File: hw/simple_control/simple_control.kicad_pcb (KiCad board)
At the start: 4 copper layers, 80 x 100 mm, 105 parts, among them J101 Screw_Terminal_01x02, J102 Jack-DC, J103 Screw_Terminal_01x03, J104 Screw_Terminal_01x03, J1301 Micro_SD_Card, J1401 Conn_02x05_Odd_Even, J601 Conn_01x04, J602 Raspberry_Pi_0_2_3, J603 Conn_01x03, Q1001 BC817, Q201 AOSP21357, Q701 BC817, Q801 BC817, Q901 BC817, SW1801 SW_Push, SW1901 SW_Push, SW2001 SW_Push, SW2101 SW_Push, SW602 SW_Push, U1101 CAT24C256, U1501 4050, U301 SN74AHCT125D, U601 PicoW

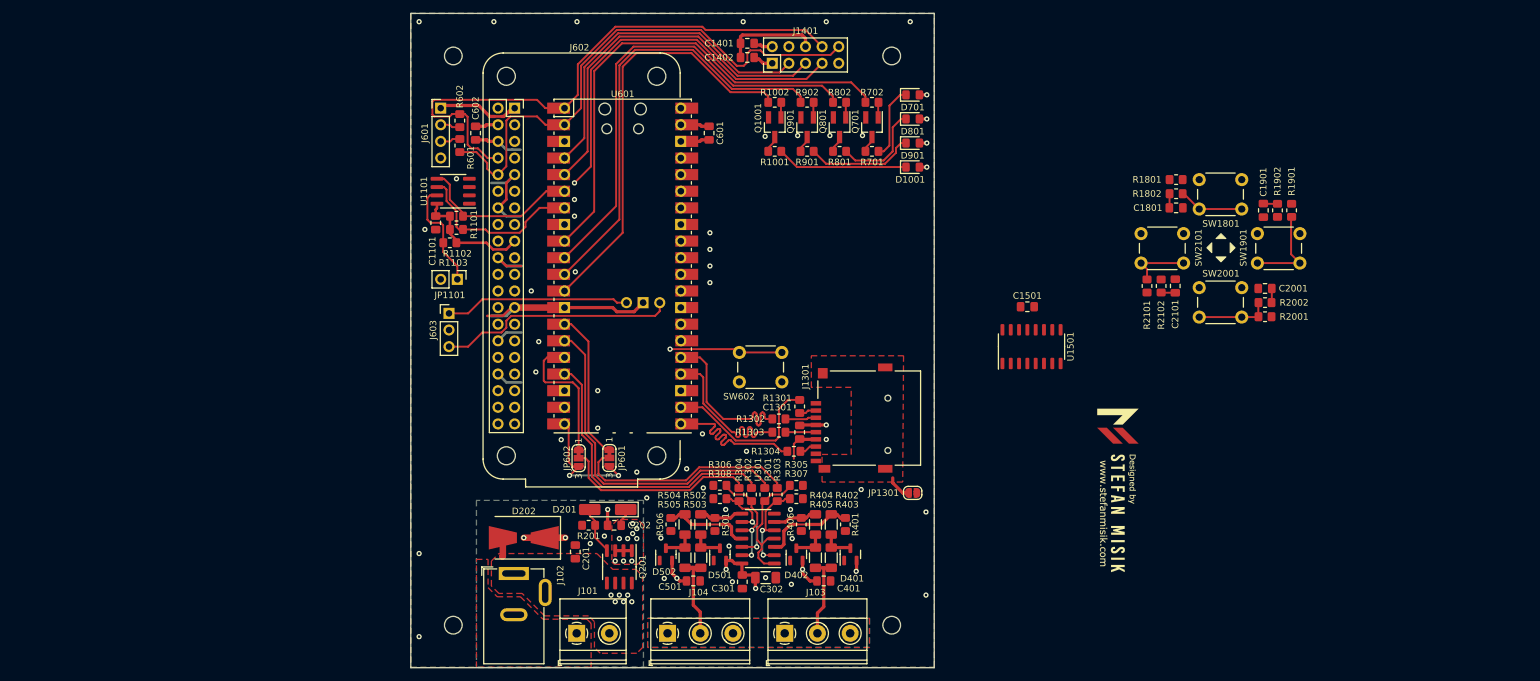
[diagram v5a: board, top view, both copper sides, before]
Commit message: chore(hw): move reset button, improve power traces, keepout near wifi antenna
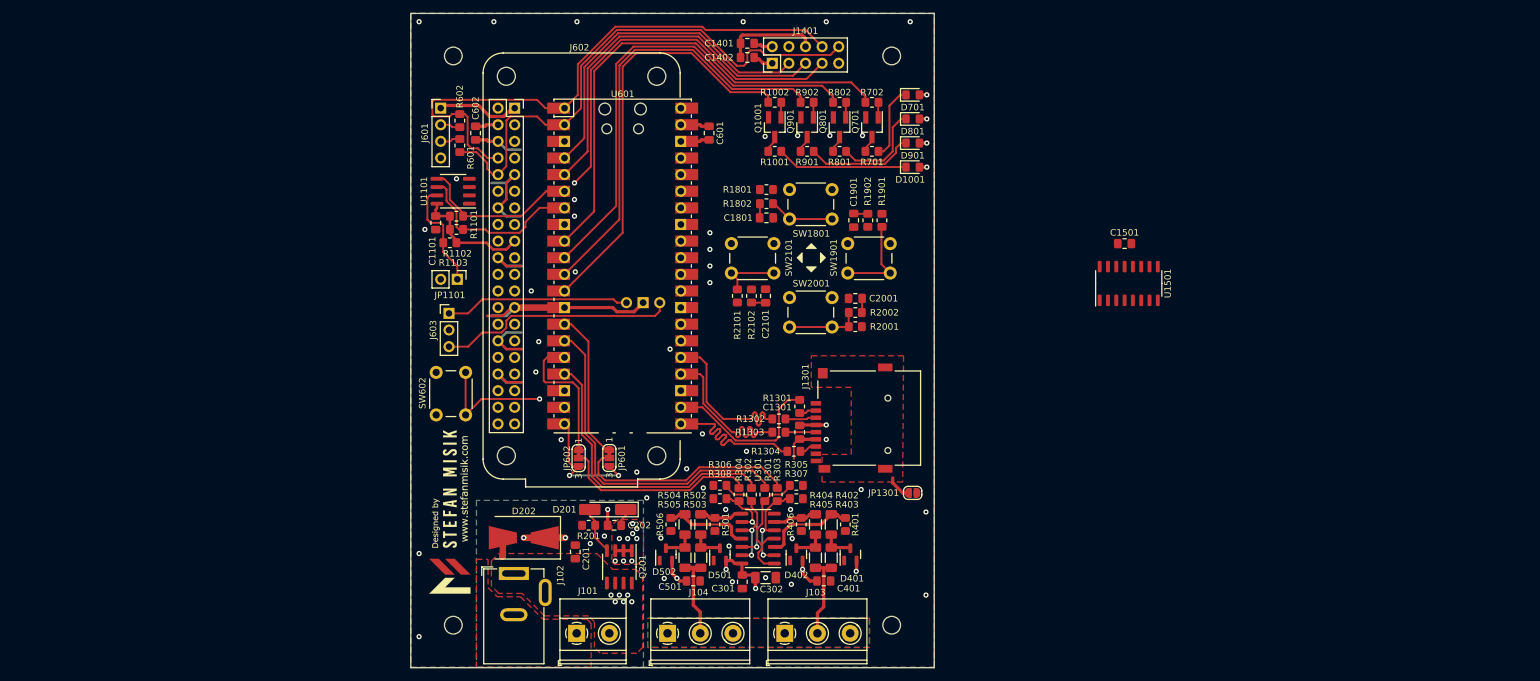
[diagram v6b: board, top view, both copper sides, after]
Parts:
- moved LOGO101 102.2 mm to (107.6, 116.8), turned to 90 degrees
- moved C1801 62.6 mm to (156.0, 71.9)
- moved C2001 62.6 mm to (169.5, 84.2)
- moved R1801 62.6 mm to (156.0, 67.6)
- moved R1802 62.6 mm to (156.0, 69.7)
- moved R1902 62.6 mm to (171.4, 72.3)
- moved R2001 62.6 mm to (169.5, 88.5)
- moved R2002 62.6 mm to (169.5, 86.4)
- moved R2101 62.6 mm to (151.5, 83.8)
- moved R2102 62.6 mm to (153.7, 83.8)
- moved SW1901 62.6 mm to (168.4, 75.8)
- moved SW2101 62.6 mm to (150.6, 75.8)
- moved C1901 62.6 mm to (169.3, 72.3)
- moved C2101 62.6 mm to (155.8, 83.8)
- moved R1901 62.6 mm to (173.6, 72.3)
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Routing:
- net Net-(U601-RUN): track 30.0 -> 54.8 mm, vias 1 -> 2
- net GND: track 101.6 -> 110.1 mm, vias 43 -> 41

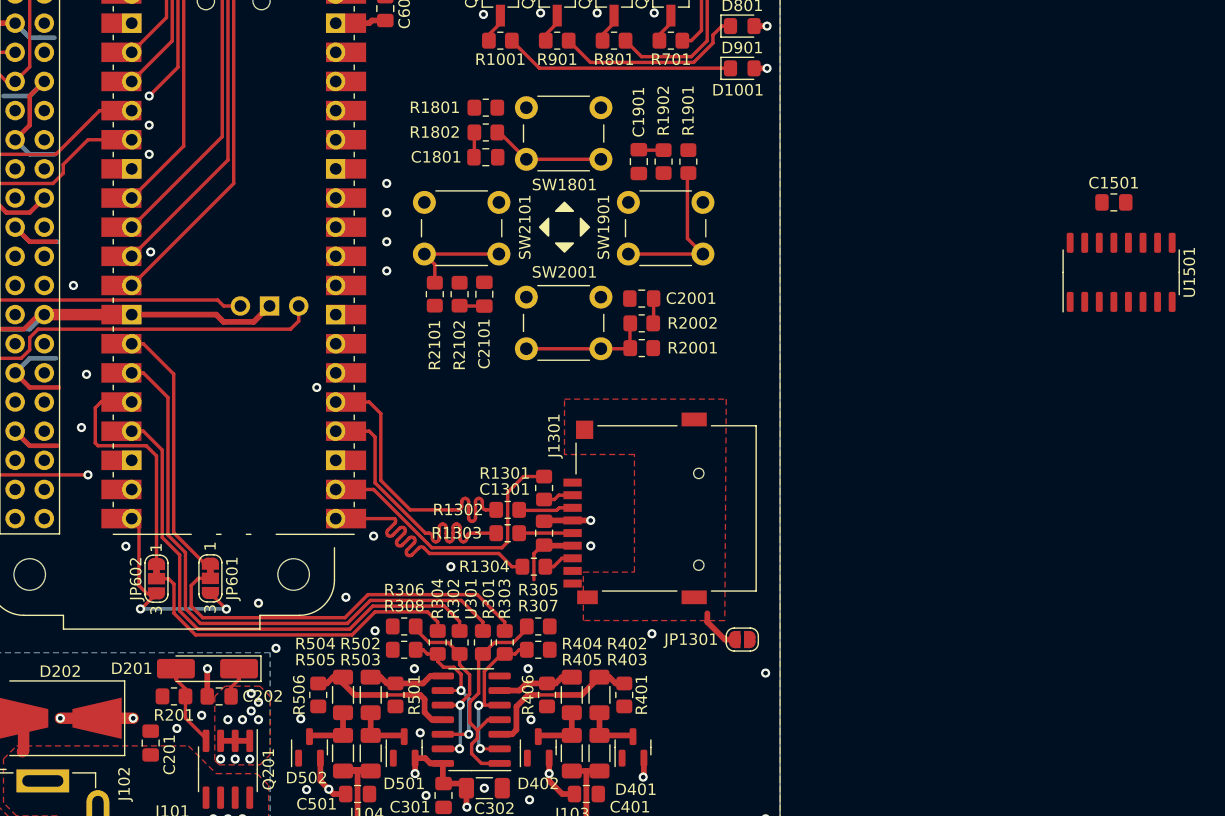
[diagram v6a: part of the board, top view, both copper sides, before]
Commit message: chore(hw): keypad layout
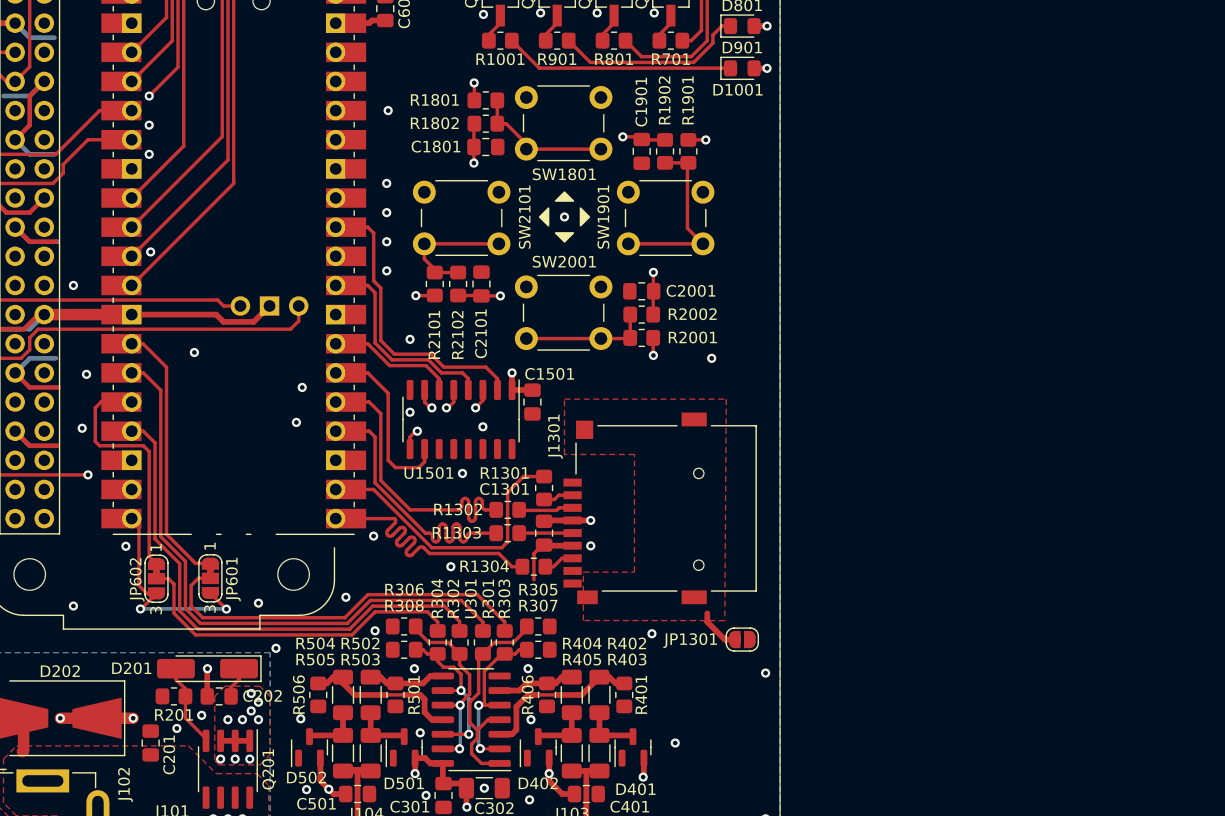
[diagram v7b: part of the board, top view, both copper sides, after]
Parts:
- moved U1501 58.9 mm to (153.8, 94.7), turned to -90 degrees
- moved C1501 53.6 mm to (160.0, 93.2), turned to -90 degrees
- moved C1901 0.92 mm to (169.5, 71.4)
- moved C2101 0.92 mm to (155.6, 82.9)
- moved R1902 0.90 mm to (171.6, 71.4)
- moved R2102 0.90 mm to (153.5, 82.9)
- moved C1801 0.89 mm to (156.0, 71.0)
- moved R1901 0.89 mm to (173.6, 71.4)
- moved R2001 0.89 mm to (169.5, 87.6)
- moved R2101 0.89 mm to (151.5, 82.9)
- moved SW1801 0.89 mm to (159.5, 66.7)
- moved SW1901 0.89 mm to (168.4, 74.9)
- moved SW2001 0.89 mm to (159.5, 83.2)
- moved SW2101 0.89 mm to (150.6, 74.9)
- moved R1802 0.76 mm to (156.0, 69.0)
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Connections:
- J602 pad 29: /CPU/BUTTON0 -> /CPU/BUTTON1
- J602 pad 31: /CPU/BUTTON1 -> /CPU/BUTTON2
- J602 pad 35: /CPU/BUTTON3 -> /CPU/BUTTON0
- J602 pad 40: /CPU/BUTTON2 -> /CPU/BUTTON3
- U601 pad 26: /CPU/BUTTON2 -> /CPU/BUTTON3
- U601 pad 27: /CPU/BUTTON1 -> /CPU/BUTTON2
- U601 pad 29: /CPU/BUTTON0 -> /CPU/BUTTON1
- U601 pad 31: /CPU/BUTTON3 -> /CPU/BUTTON0
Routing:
- net /CPU/Keypad/Filtered Button 0/SW: track 2.17 -> 58.6 mm, vias 0 -> 2
- net +3.3V: track 78.9 -> 135.2 mm, vias 1 -> 6
- net /CPU/Keypad/Filtered Button 1/SW: track 2.17 -> 44.5 mm, vias 0 -> 2
- net /CPU/BUTTON0: track 28.6 -> 67.4 mm, vias 0 -> 1
- net /CPU/Keypad/Filtered Button 2/SW: track 2.17 -> 31.1 mm, vias 0 -> 2
- net /CPU/BUTTON1: track 27.5 -> 47.0 mm
- net /CPU/Keypad/Filtered Button 3/SW: track 2.17 -> 20.4 mm, vias 0 -> 2
- net /CPU/BUTTON3: track 41.7 -> 51.7 mm
- net /CPU/BUTTON2: track 36.1 -> 38.8 mm, vias 1 -> 0
- net Net-(R1801-Pad2): track 10.0 -> 12.3 mm
- net Net-(R1901-Pad2): track 14.1 -> 16.2 mm
- net Net-(R2101-Pad2): track 9.38 -> 11.4 mm
- net Net-(U601-RUN): track 54.8 -> 54.1 mm
- net GND: vias 41 -> 52

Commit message: chore(hw): add rounded corners and dimensions
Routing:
- net GND: vias 52 -> 50
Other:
- outline, holes or cut-outs redrawn
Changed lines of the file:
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@@
     )
     (stroke (width 0.15) (type solid)) (fill solid) (layer "F.SilkS"))
-  (gr_rect (start 101.6 40.64) (end 181.6 140.64)
-    (stroke (width 0.1) (type default)) (fill none) (layer "Edge.Cuts"))
+  (gr_line (start 101.6 47.14) (end 101.6 134.14)
+    (stroke (width 0.1) (type default)) (layer "Edge.Cuts"))
+  (gr_arc (start 175.1 40.64) (mid 179.696194 42.543806) (end 181.6 47.14)
+    (stroke (width 0.1) (type default)) (layer "Edge.Cuts"))
+  (gr_arc (start 108.1 140.64) (mid 103.503806 138.736194) (end 101.6 134.14)
+    (stroke (width 0.1) (type default)) (layer "Edge.Cuts"))
+  (gr_arc (start 181.6 134.14) (mid 179.696194 138.736194) (end 175.1 140.64)
+    (stroke (width 0.1) (type default)) (layer "Edge.Cuts"))
+  (gr_line (start 181.6 134.14) (end 181.6 47.14)
+    (stroke (width 0.1) (type default)) (layer "Edge.Cuts"))
+  (gr_line (start 175.1 40.64) (end 108.1 40.64)
+    (stroke (width 0.1) (type default)) (layer "Edge.Cuts"))
+  (gr_arc (start 101.6 47.14) (mid 103.503806 42.543806) (end 108.1 40.64)
+    (stroke (width 0.1) (type default)) (layer "Edge.Cuts"))
+  (gr_line (start 108.1 140.64) (end 175.1 140.64)
+    (stroke (width 0.1) (type default)) (layer "Edge.Cuts"))
+  (dimension (type aligned) (layer "Eco1.User")
+    (pts (xy 108.1 40.64) (xy 108.1 140.64))
+    (height 10.309999)
+    (gr_text "100.0 mm" (at 96.640001 90.64 90) (layer "Eco1.User")
+      (effects (font (size 1 1) (thickness 0.15)))
+    )
+    (format (prefix "") (suffix "") (units 2) (units_format 1) (precision 1))
+    (style (thickness 0.1) (arrow_length 1.27) (text_position_mode 0) (extension_height 0.58642) (extension_offset 7) keep_text_aligned)
+  )
+  (dimension (type aligned) (layer "Eco1.User")
+    (pts (xy 101.6 47.14) (xy 181.6 47.14))
+    (height -10.31)
+    (gr_text "80.0 mm" (at 141.6 35.68) (layer "Eco1.User")
+      (effects (font (size 1 1) (thickness 0.15)))
+    )
+    (format (prefix "") (suffix "") (units 2) (units_format 1) (precision 1))
+    (style (thickness 0.1) (arrow_length 1.27) (text_position_mode 0) (extension_height 0.58642) (extension_offset 7) keep_text_aligned)
+  )
+  (dimension (type leader) (layer "Eco1.User")
+    (pts (xy 103.503806 42.543806) (xy 97.409 36.576))
+    (gr_text "R6.5" (at 92.964 36.576) (layer "Eco1.User")
+      (effects (font (size 1 1) (thickness 0.15)))
+    )
+    (format (prefix "") (suffix "") (units 0) (units_format 0) (precision 4) (override_value "R6.5"))
+    (style (thickness 0.15) (arrow_length 1.27) (text_position_mode 0) (text_frame 0) (extension_offset 0.5))
+  )
+  (dimension (type orthogonal) (layer "Eco1.User")
+    (pts (xy 108.1 47.14) (xy 101.6 47.14))
+    (height -10.31)
+    (orientation 0)
+    (gr_text "6.5 mm" (at 104.85 34.925) (layer "Eco1.User")
+      (effects (font (size 1 1) (thickness 0.15)))
+    )
+    (format (prefix "") (suffix "") (units 2) (units_format 1) (precision 1))
+    (style (thickness 0.1) (arrow_length 1.27) (text_position_mode 2) (extension_height 0.58642) (extension_offset 7) keep_text_aligned)
+  )
+  (dimension (type orthogonal) (layer "Eco1.User")
+    (pts (xy 108.1 47.14) (xy 108.1 40.64))
+    (height -10.309999)
+    (orientation 1)
+    (gr_text "6.5 mm" (at 96.012 43.89 90) (layer "Eco1.User")
+      (effects (font (size 1 1) (thickness 0.15)))
+    )
+    (format (prefix "") (suffix "") (units 2) (units_format 1) (precision 1))
+    (style (thickness 0.1) (arrow_length 1.27) (text_position_mode 2) (extension_height 0.58642) (extension_offset 7) keep_text_aligned)
+  )
   (segment (start 115.672 120.777) (end 115.672 123.596) (width 1) (layer "F.Cu") (net 1))
   (segment (start 115.672 123.596) (end 115.57 123.698) (width 1) (layer "F.Cu") (net 1))
@@
   (via (at 130.556 88.9) (size 0.8) (drill 0.4) (layers "F.Cu" "B.Cu") (free) (net 2))
   (via (at 162.814 77.089) (size 0.8) (drill 0.4) (layers "F.Cu" "B.Cu") (free) (net 2))
-  (via (at 102.87 123.19) (size 0.8) (drill 0.4) (layers "F.Cu" "B.Cu") (free) (net 2))
   (via (at 159.639 116.459) (size 0.8) (drill 0.4) (layers "F.Cu" "B.Cu") (free) (net 2))
   (via (at 124.587 105.791) (size 0.8) (drill 0.4) (layers "F.Cu" "B.Cu") (free) (net 2))
-  (via (at 102.87 135.89) (size 0.8) (drill 0.4) (layers "F.Cu" "B.Cu") (free) (net 2))
+  (via (at 102.87 129.54) (size 0.8) (drill 0.4) (layers "F.Cu" "B.Cu") (free) (net 2))
   (via (at 131.191 120.523) (size 0.8) (drill 0.4) (layers "F.Cu" "B.Cu") (free) (net 2))
   (via (at 146.177 104.902) (size 0.8) (drill 0.4) (layers "F.Cu" "B.Cu") (free) (net 2))
@@
   (via (at 172.466 122.936) (size 0.8) (drill 0.4) (layers "F.Cu" "B.Cu") (free) (net 2))
   (via (at 159.766 127.889) (size 0.8) (drill 0.4) (layers "F.Cu" "B.Cu") (free) (net 2))
-  (via (at 177.927 41.91) (size 0.8) (drill 0.4) (layers "F.Cu" "B.Cu") (free) (net 2))
   (via (at 120.015 83.058) (size 0.8) (drill 0.4) (layers "F.Cu" "B.Cu") (free) (net 2))
   (via (at 129.032 121.666) (size 0.8) (drill 0.4) (layers "F.Cu" "B.Cu") (free) (net 2))
@@
   (via (at 149.352 87.757) (size 0.8) (drill 0.4) (layers "F.Cu" "B.Cu") (free) (net 2))
   (via (at 103.759 73.66) (size 0.8) (drill 0.4) (layers "F.Cu" "B.Cu") (free) (net 2))
-  (via (at 102.87 41.91) (size 0.8) (drill 0.4) (layers "F.Cu" "B.Cu") (free) (net 2))
+  (via (at 117.856 139.446) (size 0.8) (drill 0.4) (layers "F.Cu" "B.Cu") (free) (net 2))
   (via (at 152.908 107.569) (size 0.8) (drill 0.4) (layers "F.Cu" "B.Cu") (free) (net 2))
   (via (at 125.222 120.777) (size 0.8) (drill 0.4) (layers "F.Cu" "B.Cu") (free) (net 2))
